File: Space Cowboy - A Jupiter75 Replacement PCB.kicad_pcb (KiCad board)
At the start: 2 copper layers, 313.5 x 129.5 mm, 236 parts, among them SW1 SW_PUSH, U1 ATmega32U4-AU, Y1 16MHz

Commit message: Update Space Cowboy - A Jupiter75 Replacement PCB.kicad_pcb
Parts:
- C1, C2, C3, C4, C5, C6, C7, CRGB1, CRGB10, CRGB11, CRGB12, CRGB13, CRGB14, CRGB15, CRGB16, CRGB17, CRGB18, CRGB2, CRGB3, CRGB4, CRGB5, CRGB6, CRGB7, CRGB8, CRGB9, D1, D10, D11, D12, D13, D14, D15, D16, D17, D18, D19, D2, D20, D21, D22, D23, D24, D25, D26, D27, D28, D29, D3, D30, D31, D32, D33, D34, D35, D36, D37, D38, D39, D4, D40, D41, D42, D43, D44, D45, D46, D47, D48, D49, D5, D50, D51, D52, D53, D54, D55, D56, D57, D58, D59, D6, D60, D61, D62, D63, D64, D65, D66, D67, D68, D69, D7, D70, D71, D72, D73, D74, D75, D76, D77, D78, D79, D8, D80, D81, D82, D83, D84, D85, D9, DRGB1, DRGB10, DRGB11, DRGB12, DRGB13, DRGB14, DRGB15, DRGB16, DRGB17, DRGB18, DRGB2, DRGB3, DRGB4, DRGB5, DRGB6, DRGB7, DRGB8, DRGB9, F1, FB1, FB2, R1, R2, R3, R4, R5, R6, R7, SW1, U1, USB1, Y1: moved to B.Cu
- MX_EnterISO1: footprint Keyboard_Mine:MX-ISO -> Keyboard_Mine:MXOnly-2U
- moved D16 391.6 mm to (343.7, 64.3), turned to 90 degrees
- moved D15 374.2 mm to (324.6, 64.3), turned to 90 degrees
- moved D76 371.7 mm to (343.7, 140.5), turned to 90 degrees
- moved D14 357.8 mm to (300.8, 64.3), turned to 90 degrees
- moved D75 353.8 mm to (324.6, 140.5), turned to 90 degrees
- moved D84 347.7 mm to (324.6, 159.5), turned to 90 degrees
- moved D85 342.8 mm to (343.7, 159.5), turned to 90 degrees
- moved D60 337.3 mm to (304.8, 121.4), turned to 90 degrees
- moved D32 331.9 mm to (343.7, 83.3), turned to 90 degrees
- moved D30 330.4 mm to (305.6, 83.3), turned to 90 degrees
- moved D74 329.2 mm to (298.4, 140.5), turned to 90 degrees
- moved D13 321.3 mm to (281.8, 64.3), turned to 90 degrees
- moved D31 320.8 mm to (329.6, 83.3), turned to 90 degrees
- moved D59 320.2 mm to (281.8, 121.4), turned to 90 degrees
- moved D12 308.8 mm to (262.7, 64.3), turned to 90 degrees
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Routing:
- net ROW1: track 0.00 -> 290.1 mm
- net ROW0: track 0.00 -> 285.8 mm
- net ROW2: track 0.00 -> 282.6 mm
- net ROW4: track 0.00 -> 277.2 mm
- net ROW3: track 0.00 -> 276.6 mm
- net ROW5: track 0.00 -> 274.4 mm
- net COL0: track 0.00 -> 152.5 mm
- net COL11: track 0.00 -> 129.9 mm
- net COL6: track 0.00 -> 125.2 mm
- net COL2: track 0.00 -> 121.7 mm
- net COL12: track 0.00 -> 119.0 mm
- net COL1: track 0.00 -> 115.4 mm
- net COL10: track 0.00 -> 114.6 mm
- net COL14: track 0.00 -> 103.3 mm
- net COL15: track 0.00 -> 97.6 mm
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
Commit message: Update Space Cowboy - A Jupiter75 Replacement PCB.kicad_pcb
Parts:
- U1: footprint Keyboard_Mine:ATMEGA32U4_AU -> ATmega32U4-MUR_QFN44:QFN44G-0.5-7X7MM
- moved DRGB9 336.4 mm to (348.4, 49.4), turned to 315 degrees
- moved DRGB10 333.2 mm to (348.2, 104.8), turned to 270 degrees
- moved DRGB11 301.4 mm to (348.4, 160.0), turned to 225 degrees
- moved DRGB12 273.6 mm to (315.5, 174.4)
- moved DRGB8 272.9 mm to (269.4, 34.4)
- moved DRGB6 270.8 mm to (199.1, 35.7)
- moved DRGB13 270.1 mm to (278.4, 174.2)
- moved DRGB7 242.2 mm to (236.7, 35.7)
- moved D1 230.0 mm to (61.7, 49.4)
- moved DRGB14 223.6 mm to (236.7, 175.1)
- moved FB1 210.7 mm to (65.1, 54.8), turned to 90 degrees
- moved SW1 198.4 mm to (213.5, 152.4), turned to 0 degrees
- moved DRGB5 198.1 mm to (160.5, 36.6)
- moved FB2 197.7 mm to (69.2, 46.4), turned to 90 degrees
- moved DRGB15 193.8 mm to (202.1, 175.5)
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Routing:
- net COL13: track 68.0 -> 130.7 mm
- net Net-(FB2-Pad2): track 0.00 -> 35.9 mm
- net VBUS: track 0.00 -> 17.0 mm
- net D-: track 0.00 -> 14.4 mm
- net D+: track 0.00 -> 13.0 mm, vias 0 -> 3
- net Net-(F1-Pad2): track 0.00 -> 12.2 mm
- net Net-(D81-Pad2): track 0.00 -> 10.8 mm
- net Net-(R6-Pad1): track 0.00 -> 4.18 mm
- net Net-(R5-Pad1): track 0.00 -> 3.84 mm
- net ROW5: track 274.4 -> 272.3 mm
- net Net-(D85-Pad2): track 10.8 -> 11.4 mm
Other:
- net class Default: trace_width 0.25 -> 0.2
- rule via_min_drill: 0.3 -> 0.2
- rule via_min_size: 0.4 -> 0.45

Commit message: Update Space Cowboy - A Jupiter75 Replacement PCB.kicad_pcb
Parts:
- moved CRGB9 342.1 mm to (350.9, 46.9), turned to 135 degrees
- moved CRGB10 327.5 mm to (351.8, 104.8), turned to 90 degrees
- moved CRGB11 316.0 mm to (345.6, 157.5), turned to 45 degrees
- moved CRGB2 136.1 mm to (49.9, 51.8), turned to 225 degrees
- moved CRGB1 104.6 mm to (50.9, 104.8), turned to 270 degrees
- moved CRGB18 67.3 mm to (49.8, 157.5), turned to 315 degrees
- turned D1 to 180 degrees
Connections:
- U1 pad 1: COL13 -> Net-(U1-Pad1)
- U1 pad 10: Net-(U1-Pad10) -> ROW4
- U1 pad 11: COL0 -> ROW3
- U1 pad 12: COL4 -> Net-(R7-Pad2)
- U1 pad 18: COL7 -> ROW2
- U1 pad 19: COL8 -> ROW1
- U1 pad 20: COL9 -> ROW0
- U1 pad 21: ROW1 -> COL15
- U1 pad 22: ROW0 -> COL14
- U1 pad 25: COL10 -> COL13
- U1 pad 26: COL11 -> COL12
- U1 pad 27: COL12 -> COL11
- U1 pad 28: COL1 -> COL10
- U1 pad 29: COL2 -> COL9
- U1 pad 30: COL3 -> COL8
- U1 pad 31: COL5 -> COL7
- U1 pad 36: ROW5 -> COL5
- U1 pad 37: ROW4 -> COL4
- U1 pad 38: ROW3 -> COL3
- U1 pad 39: ROW2 -> COL2
- U1 pad 40: COL15 -> COL1
- U1 pad 41: COL14 -> COL0
- U1 pad 9: Net-(R7-Pad2) -> ROW5
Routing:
- net (no net): track 0.00 -> 85.0 mm
- net GND: track 0.00 -> 11.4 mm
- net +5V: track 0.00 -> 5.91 mm
- net VBUS: track 17.0 -> 12.8 mm
- net D-: track 14.4 -> 10.9 mm
- net D+: track 13.0 -> 12.6 mm, vias 3 -> 0
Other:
- net class Default: via_dia 0.8 -> 0.45

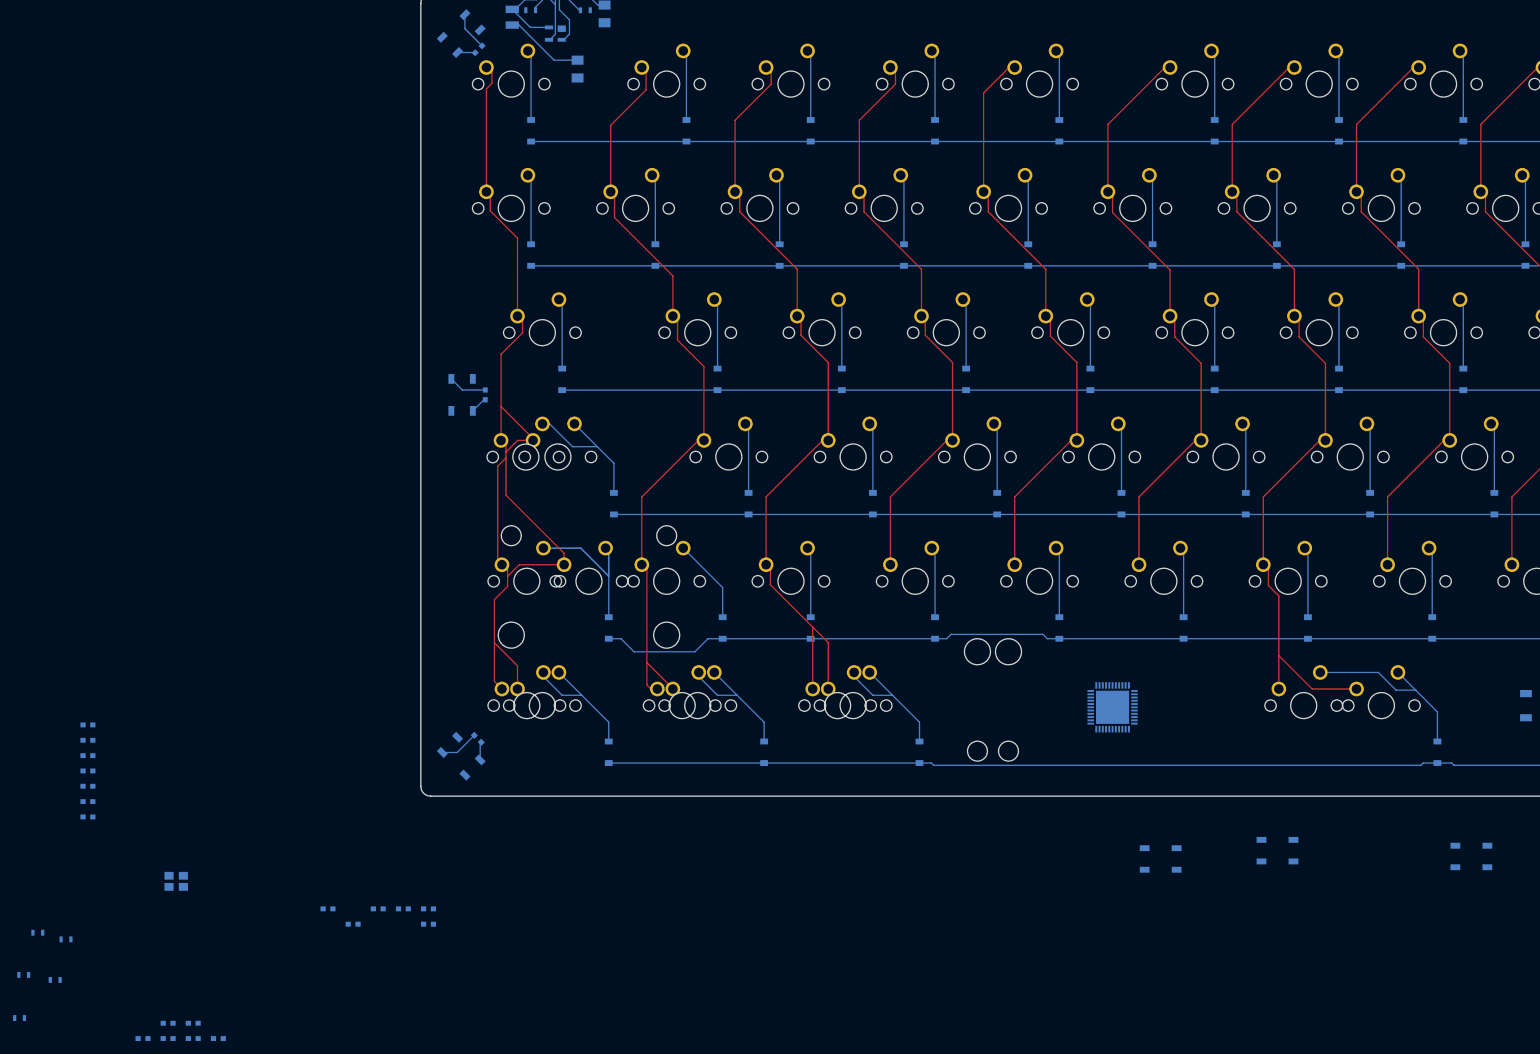
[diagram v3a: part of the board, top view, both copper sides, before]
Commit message: Update Space Cowboy - A Jupiter75 Replacement PCB.kicad_pcb
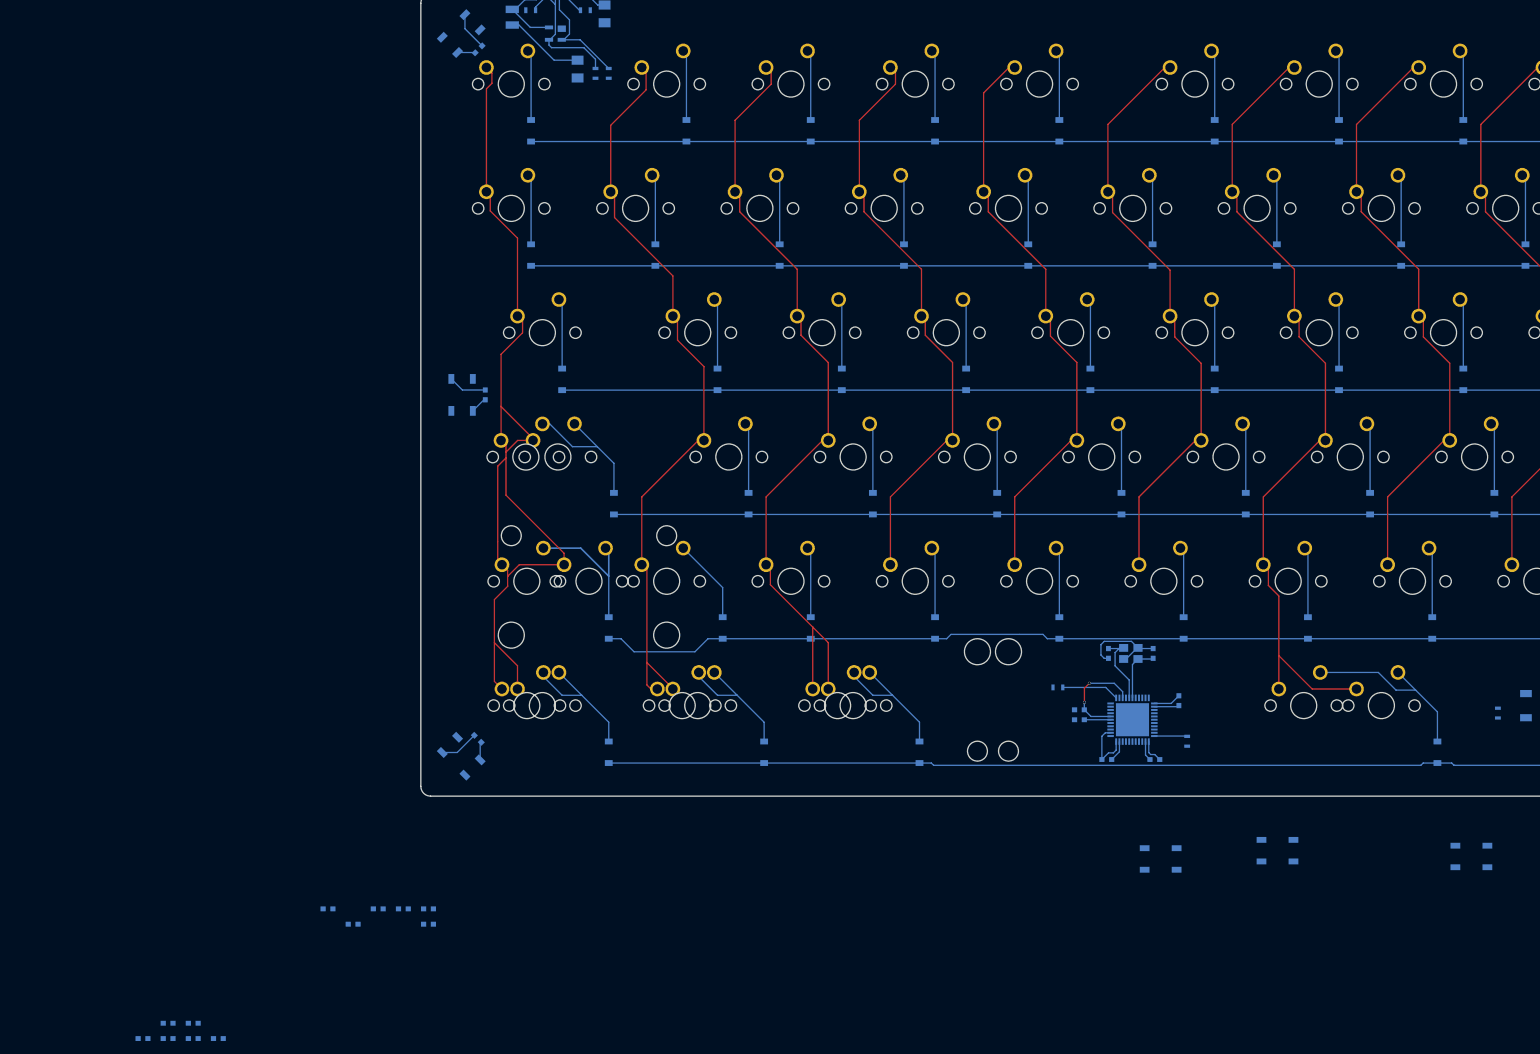
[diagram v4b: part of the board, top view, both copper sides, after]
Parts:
- moved R4 224.9 mm to (206.1, 153.5), turned to 90 degrees
- moved R1 178.6 mm to (158.5, 157.9), turned to 270 degrees
- moved C3 167.3 mm to (157.2, 151.6), turned to 90 degrees
- moved R7 167.0 mm to (138.7, 149.6)
- moved C6 164.5 mm to (153.3, 144.4), turned to 270 degrees
- moved C2 163.6 mm to (153.5, 160.7), turned to 180 degrees
- moved R3 163.6 mm to (67.8, 55.5), turned to 90 degrees
- moved C7 158.4 mm to (146.4, 144.4), turned to 270 degrees
- moved R2 156.6 mm to (69.8, 55.5), turned to 270 degrees
- moved C5 156.2 mm to (146.2, 160.7), turned to 180 degrees
- moved C4 152.1 mm to (142.0, 153.0), turned to 180 degrees
- moved C1 152.0 mm to (142.0, 154.6)
- moved Y1 150.4 mm to (149.9, 144.4), turned to 180 degrees
- moved U1 3.59 mm to (150.1, 154.6)
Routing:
- net +5V: track 5.91 -> 38.2 mm, vias 0 -> 2
- net GND: track 11.4 -> 36.5 mm
- net Net-(C7-Pad1): track 0.00 -> 11.8 mm
- net D-: track 10.9 -> 21.1 mm
- net D+: track 12.6 -> 21.7 mm
- net Net-(R7-Pad2): track 0.00 -> 8.84 mm
- net Net-(C6-Pad2): track 0.00 -> 8.68 mm
- net Net-(R1-Pad1): track 0.00 -> 5.05 mm
- net Net-(C1-Pad2): track 0.00 -> 4.03 mm

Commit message: Update Space Cowboy - A Jupiter75 Replacement PCB.kicad_pcb
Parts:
- added C8: 0.1uF, Capacitors_SMD:C_0603, B.Cu at (142.9, 145.8)
- moved C4 0.13 mm to (142.0, 153.2)
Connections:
- DRGB1 pad 1VDD: (no net) -> +5V
- DRGB1 pad 3GND: (no net) -> GND
- DRGB10 pad 1VDD: (no net) -> +5V
- DRGB10 pad 3GND: (no net) -> GND
- DRGB11 pad 1VDD: (no net) -> +5V
- DRGB11 pad 3GND: (no net) -> GND
- DRGB12 pad 1VDD: (no net) -> +5V
- DRGB12 pad 3GND: (no net) -> GND
- DRGB13 pad 1VDD: (no net) -> +5V
- DRGB13 pad 3GND: (no net) -> GND
- DRGB14 pad 1VDD: (no net) -> +5V
- DRGB14 pad 3GND: (no net) -> GND
- DRGB15 pad 1VDD: (no net) -> +5V
- DRGB15 pad 3GND: (no net) -> GND
- DRGB16 pad 1VDD: (no net) -> +5V
- DRGB16 pad 3GND: (no net) -> GND
- DRGB17 pad 1VDD: (no net) -> +5V
- DRGB17 pad 3GND: (no net) -> GND
- DRGB18 pad 1VDD: (no net) -> +5V
- DRGB18 pad 3GND: (no net) -> GND
- DRGB2 pad 1VDD: (no net) -> +5V
- DRGB2 pad 3GND: (no net) -> GND
- DRGB3 pad 1VDD: (no net) -> +5V
- DRGB3 pad 3GND: (no net) -> GND
- DRGB4 pad 1VDD: (no net) -> +5V
- DRGB4 pad 3GND: (no net) -> GND
- DRGB5 pad 1VDD: (no net) -> +5V
- DRGB5 pad 3GND: (no net) -> GND
- DRGB6 pad 1VDD: (no net) -> +5V
- DRGB6 pad 3GND: (no net) -> GND
- DRGB7 pad 1VDD: (no net) -> +5V
- DRGB7 pad 3GND: (no net) -> GND
- DRGB8 pad 1VDD: (no net) -> +5V
- DRGB8 pad 3GND: (no net) -> GND
- DRGB9 pad 1VDD: (no net) -> +5V
- DRGB9 pad 3GND: (no net) -> GND
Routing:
- net +5V: track 38.2 -> 294.1 mm, vias 2 -> 7
- net Net-(R3-Pad1): track 0.00 -> 193.5 mm, vias 0 -> 2
- net Net-(R2-Pad2): track 0.00 -> 192.5 mm, vias 0 -> 2
- net GND: track 36.5 -> 71.3 mm
- net (no net): track 85.0 -> 50.4 mm
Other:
- net class Power added: clearance 0.2, trace_width 0.25, via_dia 0.45, via_drill 0.4

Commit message: Update Space Cowboy - A Jupiter75 Replacement PCB.kicad_pcb
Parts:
- moved CRGB12 5.55 mm to (21.8, 181.2)
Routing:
- net GND: track 71.3 -> 92.6 mm, vias 0 -> 2
- net VBUS: track 12.7 -> 20.2 mm
- net Net-(FB2-Pad2): track 35.9 -> 33.9 mm
- net ROW4: track 277.2 -> 278.7 mm
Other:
- net class Power: trace_width 0.25 -> 0.382
- net class Power Narrow added: clearance 0.2, trace_width 0.3, via_dia 0.45, via_drill 0.4
